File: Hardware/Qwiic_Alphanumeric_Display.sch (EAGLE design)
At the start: 33 parts, among them J4 Vertical Qwiic Connector, J5 Vertical Qwiic Connector, U2 XC9140

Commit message: Add prod_id to new LED mapping IC
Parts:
- IC1: PROD_ID (none) -> IC-16176
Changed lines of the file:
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@@
 <part name="H2" library="SparkFun-Hardware" deviceset="STAND-OFF" device=""/>
 <part name="IC1" library="Alphanumeric_Display_Library" deviceset="VK16K33" device="VK16K33">
-<attribute name="PROD_ID" value=""/>
+<attribute name="PROD_ID" value="IC-16176"/>
 </part>
 <part name="H3" library="SparkFun-Hardware" deviceset="STAND-OFF" device=""/>

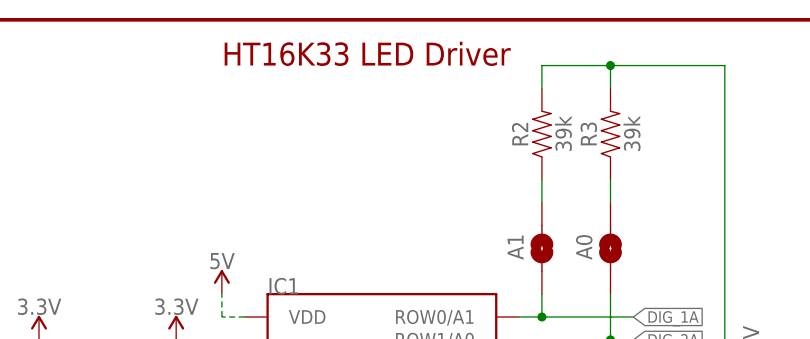
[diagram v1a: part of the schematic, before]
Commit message: Update mounting hole placement and measures
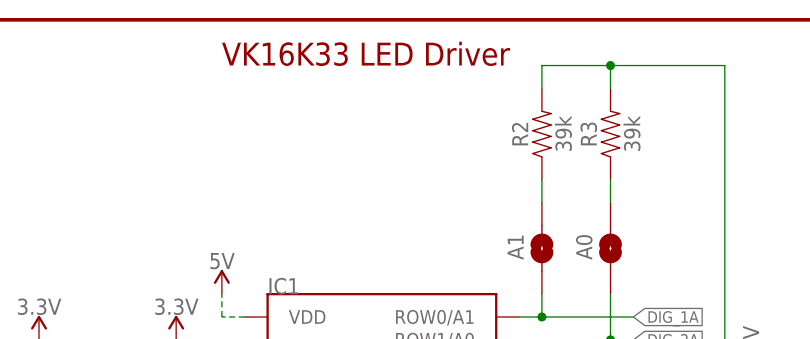
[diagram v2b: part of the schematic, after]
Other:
- note added: "VK16K33 LED Driver"
- note removed: "HT16K33 LED Driver"
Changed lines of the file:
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@@
 <wire x1="55.88" y1="185.42" x2="55.88" y2="66.04" width="0.2032" layer="97" style="longdash"/>
 <text x="195.58" y="129.54" size="2.54" layer="94" font="vector">Alphanumeric Display</text>
-<text x="104.14" y="180.34" size="2.54" layer="94" font="vector">HT16K33 LED Driver</text>
+<text x="104.14" y="180.34" size="2.54" layer="94" font="vector">VK16K33 LED Driver</text>
 <text x="10.16" y="180.34" size="2.54" layer="94" font="vector">3.3V to 5V boost circuit</text>
 <text x="109.22" y="96.52" size="1.27" layer="97" font="vector">VK16K33</text>

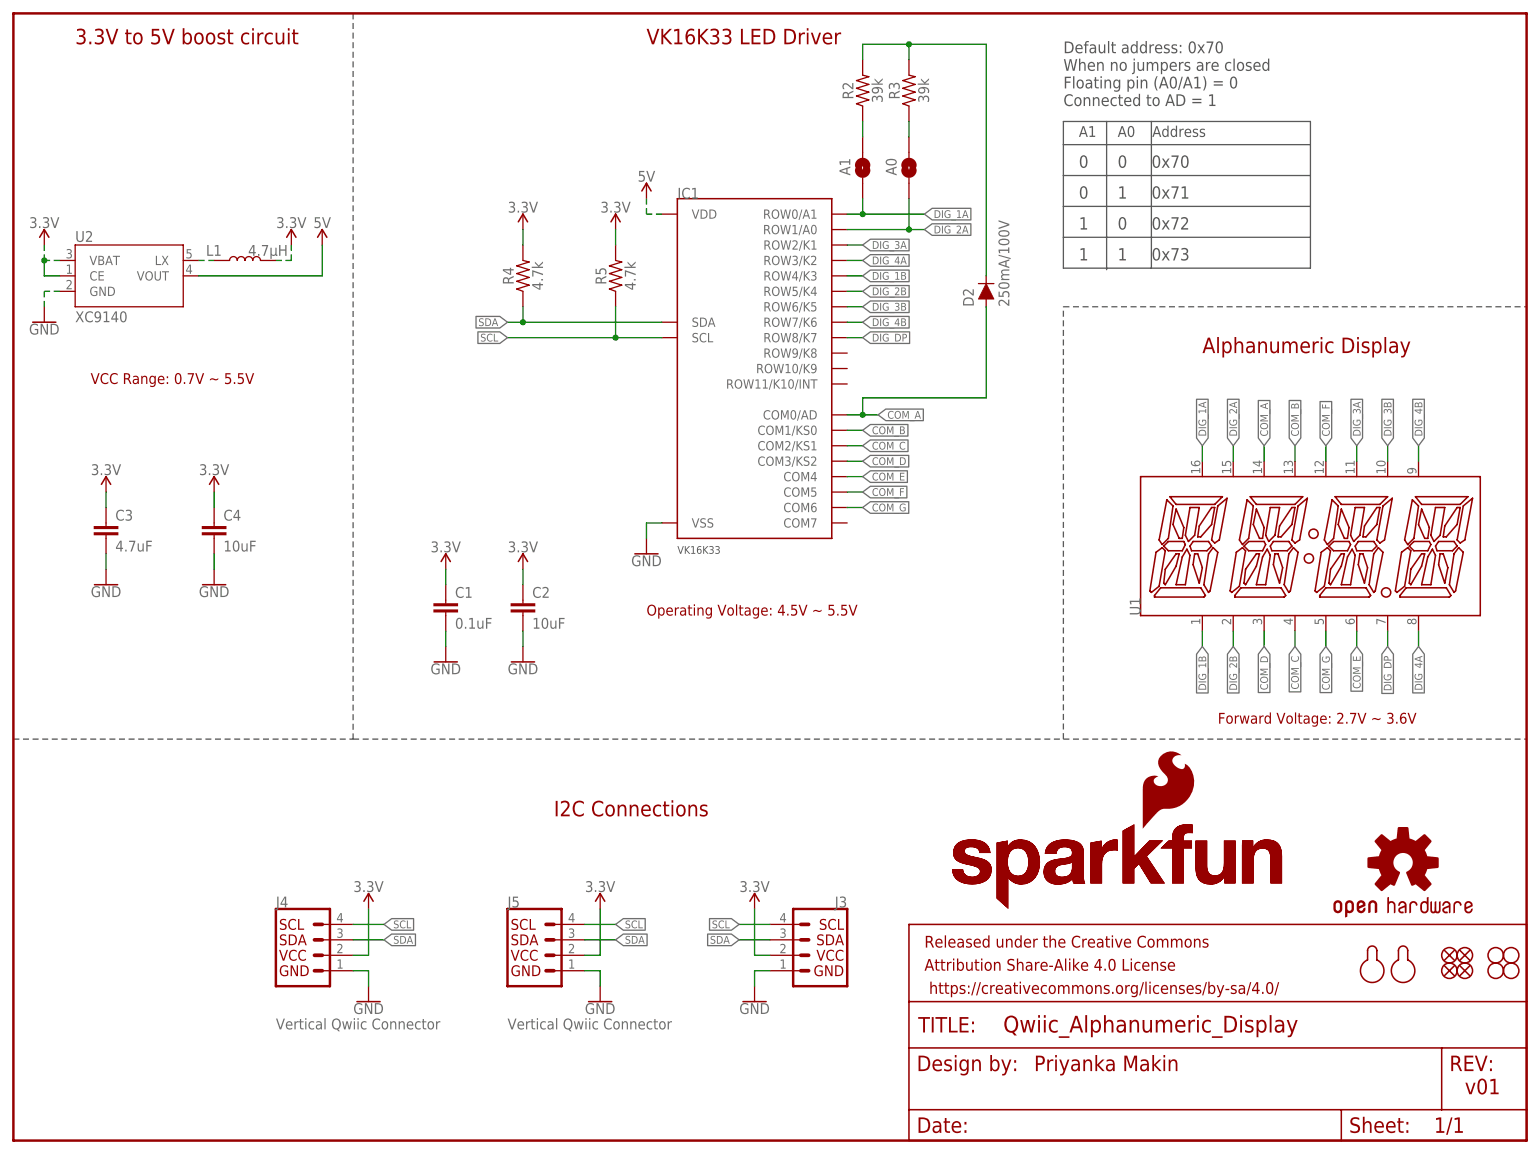
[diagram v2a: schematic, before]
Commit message: Added test point to 5V rail
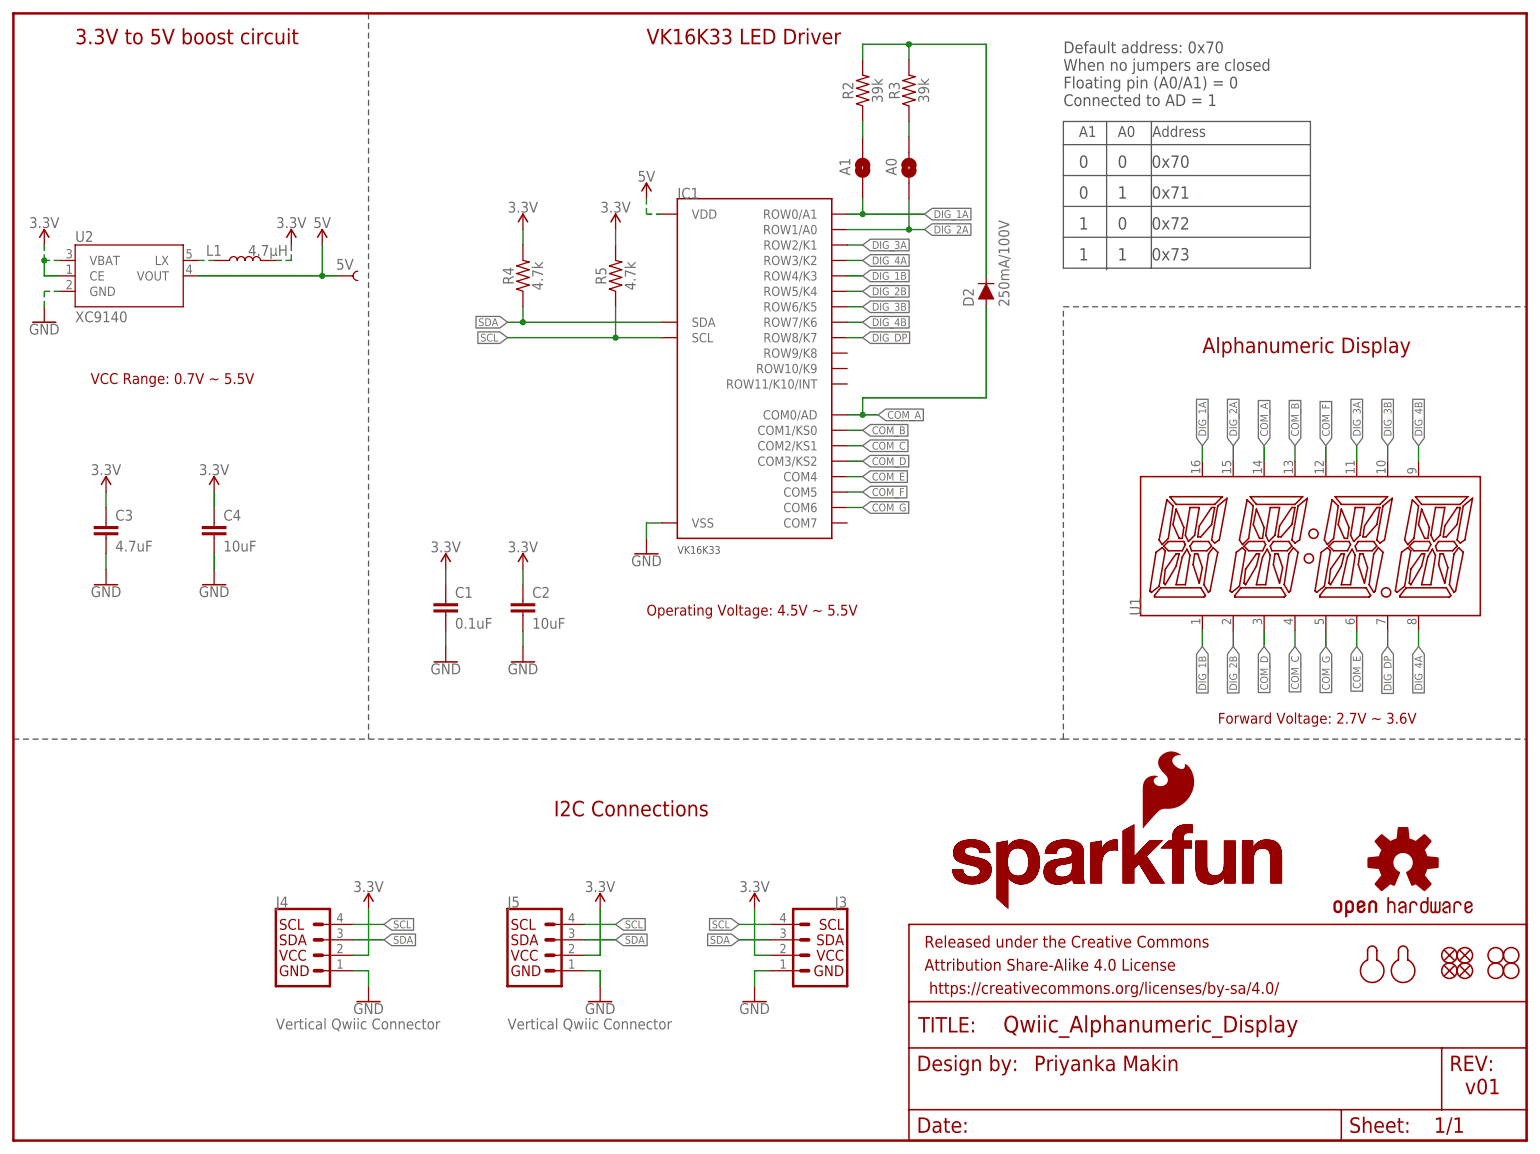
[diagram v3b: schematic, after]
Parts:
- added 5V: TEST-POINT3, SparkFun-Connectors:TEST-POINT3
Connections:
- net 5V: now also 5V.1
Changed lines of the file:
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@@
 <part name="SUPPLY1" library="SparkFun-PowerSymbols" deviceset="3.3V" device=""/>
 <part name="SUPPLY9" library="SparkFun-PowerSymbols" deviceset="3.3V" device=""/>
+<part name="5V" library="SparkFun-Connectors" deviceset="TEST-POINT" device="3"/>
 </parts>
 <sheets>
@@
 <plain>
 <text x="167.894" y="11.43" size="2.54" layer="94" font="vector">Priyanka Makin</text>
-<wire x1="0" y1="66.04" x2="55.88" y2="66.04" width="0.2032" layer="97" style="longdash"/>
+<wire x1="0" y1="66.04" x2="58.42" y2="66.04" width="0.2032" layer="97" style="longdash"/>
 <text x="88.9" y="53.34" size="2.54" layer="94" font="vector">I2C Connections</text>
 <text x="175.26" y="165.1" size="1.778" layer="97" font="vector">A1     A0    Address</text>
@@
 <text x="175.26" y="149.86" size="2.032" layer="97" font="vector">1      0     0x72</text>
 <text x="175.26" y="144.78" size="2.032" layer="97" font="vector">1      1     0x73</text>
-<wire x1="55.88" y1="66.04" x2="172.72" y2="66.04" width="0.2032" layer="97" style="longdash"/>
+<wire x1="58.42" y1="66.04" x2="172.72" y2="66.04" width="0.2032" layer="97" style="longdash"/>
 <wire x1="172.72" y1="66.04" x2="248.92" y2="66.04" width="0.2032" layer="97" style="longdash"/>
 <wire x1="172.72" y1="167.64" x2="172.72" y2="163.83" width="0.2032" layer="97"/>
@@
 <wire x1="172.72" y1="66.04" x2="172.72" y2="137.16" width="0.2032" layer="97" style="longdash"/>
 <wire x1="172.72" y1="137.16" x2="248.92" y2="137.16" width="0.2032" layer="97" style="longdash"/>
-<wire x1="55.88" y1="185.42" x2="55.88" y2="66.04" width="0.2032" layer="97" style="longdash"/>
+<wire x1="58.42" y1="185.42" x2="58.42" y2="66.04" width="0.2032" layer="97" style="longdash"/>
 <text x="195.58" y="129.54" size="2.54" layer="94" font="vector">Alphanumeric Display</text>
 <text x="104.14" y="180.34" size="2.54" layer="94" font="vector">VK16K33 LED Driver</text>
@@
 <attribute name="VALUE" x="99.06" y="152.654" size="1.778" layer="96" align="bottom-center"/>
 </instance>
+<instance part="5V" gate="G$1" x="53.34" y="142.24" smashed="yes">
+<attribute name="NAME" x="53.086" y="143.256" size="1.778" layer="95" font="vector"/>
+</instance>
 </instances>
 <busses>
@@
 <wire x1="30.48" y1="142.24" x2="50.8" y2="142.24" width="0.1524" layer="91"/>
 <wire x1="50.8" y1="142.24" x2="50.8" y2="147.32" width="0.1524" layer="91"/>
-</segment>
-</net>
+<pinref part="5V" gate="G$1" pin="1"/>
+<wire x1="53.34" y1="142.24" x2="50.8" y2="142.24" width="0.1524" layer="91"/>
+<junction x="50.8" y="142.24"/>
+</segment>
+</net>

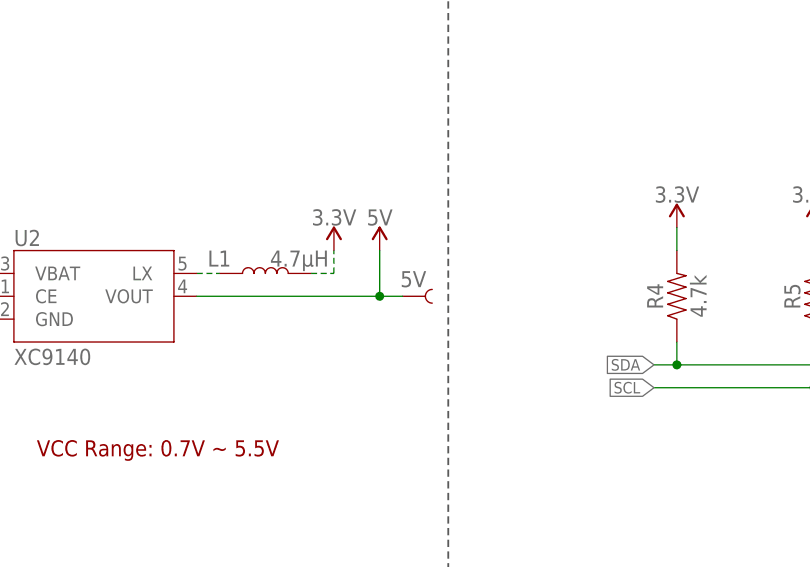
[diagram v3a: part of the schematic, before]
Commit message: Remove the 5V test point after all!
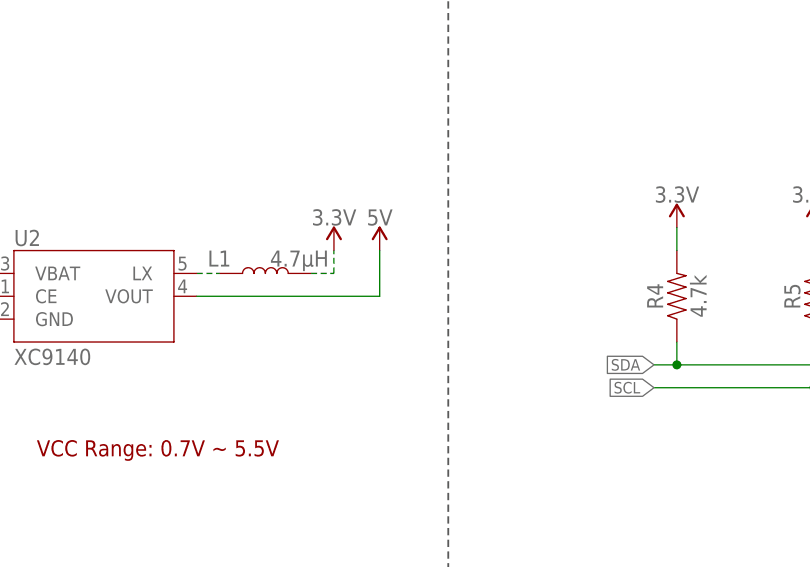
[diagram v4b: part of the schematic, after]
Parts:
- removed 5V: TEST-POINT3, SparkFun-Connectors:TEST-POINT3
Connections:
- net 5V: no longer 5V.1
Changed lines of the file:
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@@
 <part name="SUPPLY1" library="SparkFun-PowerSymbols" deviceset="3.3V" device=""/>
 <part name="SUPPLY9" library="SparkFun-PowerSymbols" deviceset="3.3V" device=""/>
-<part name="5V" library="SparkFun-Connectors" deviceset="TEST-POINT" device="3"/>
 </parts>
 <sheets>
@@
 <attribute name="VALUE" x="99.06" y="152.654" size="1.778" layer="96" align="bottom-center"/>
 </instance>
-<instance part="5V" gate="G$1" x="53.34" y="142.24" smashed="yes">
-<attribute name="NAME" x="53.086" y="143.256" size="1.778" layer="95" font="vector"/>
-</instance>
 </instances>
 <busses>
@@
 <wire x1="30.48" y1="142.24" x2="50.8" y2="142.24" width="0.1524" layer="91"/>
 <wire x1="50.8" y1="142.24" x2="50.8" y2="147.32" width="0.1524" layer="91"/>
-<pinref part="5V" gate="G$1" pin="1"/>
-<wire x1="53.34" y1="142.24" x2="50.8" y2="142.24" width="0.1524" layer="91"/>
-<junction x="50.8" y="142.24"/>
-</segment>
-</net>
+</segment>
+</net>
